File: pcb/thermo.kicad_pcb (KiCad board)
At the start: 2 copper layers, 123.2 x 91.4 mm, 38 parts, among them J1 DB15_Female, J2 Barrel_Jack, U1 BME280

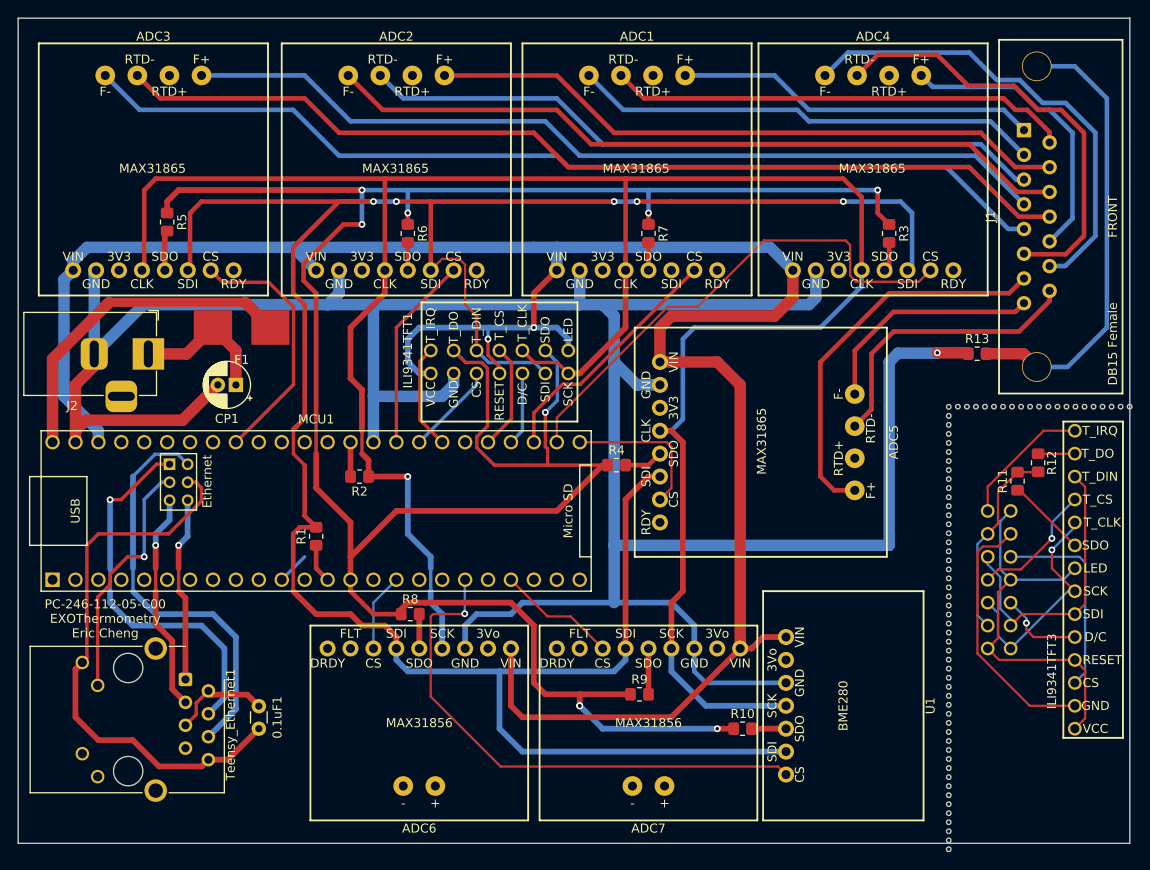
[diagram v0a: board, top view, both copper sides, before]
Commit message: removed acid trap and made some tracer wider
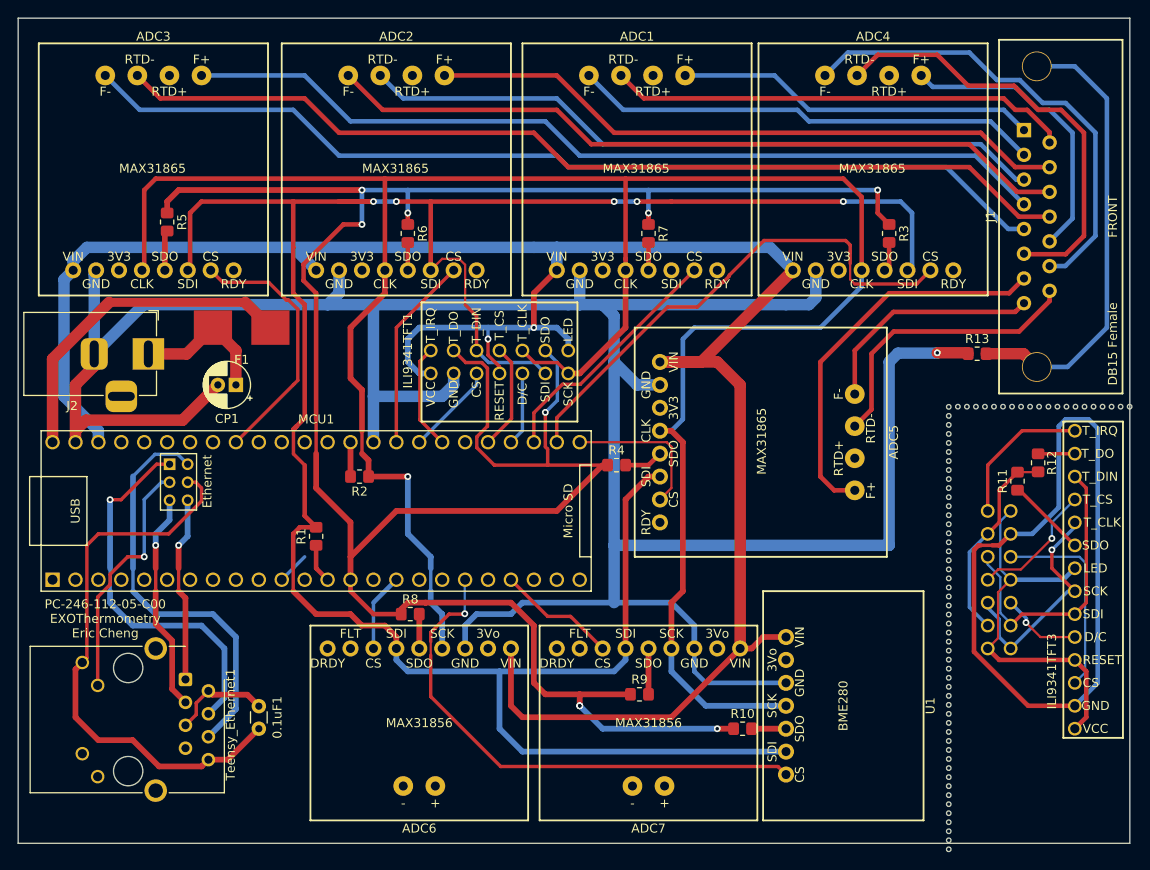
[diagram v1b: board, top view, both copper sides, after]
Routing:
- net GND: track 332.1 -> 385.3 mm
- net +3V3: track 295.1 -> 291.2 mm
- net /SDI: track 315.5 -> 313.5 mm
- net /CS_4: track 56.7 -> 58.4 mm
- net /T_IRQ: track 26.6 -> 28.0 mm
- net /CS_8: track 59.6 -> 58.6 mm
- net /SDO: track 300.6 -> 301.3 mm
- net /CS_3: track 28.5 -> 29.0 mm

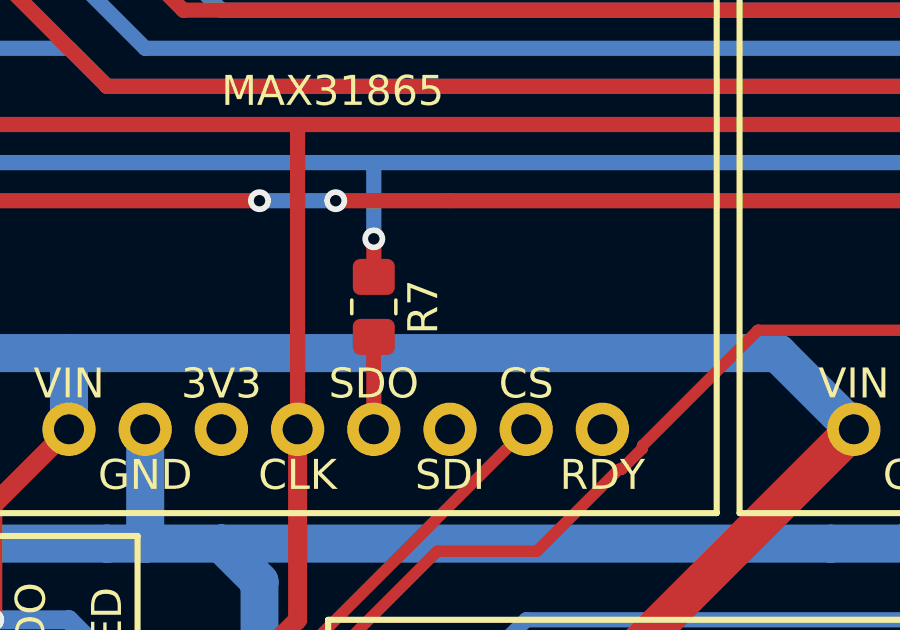
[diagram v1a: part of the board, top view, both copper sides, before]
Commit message: added missing SDI trace for ADC1
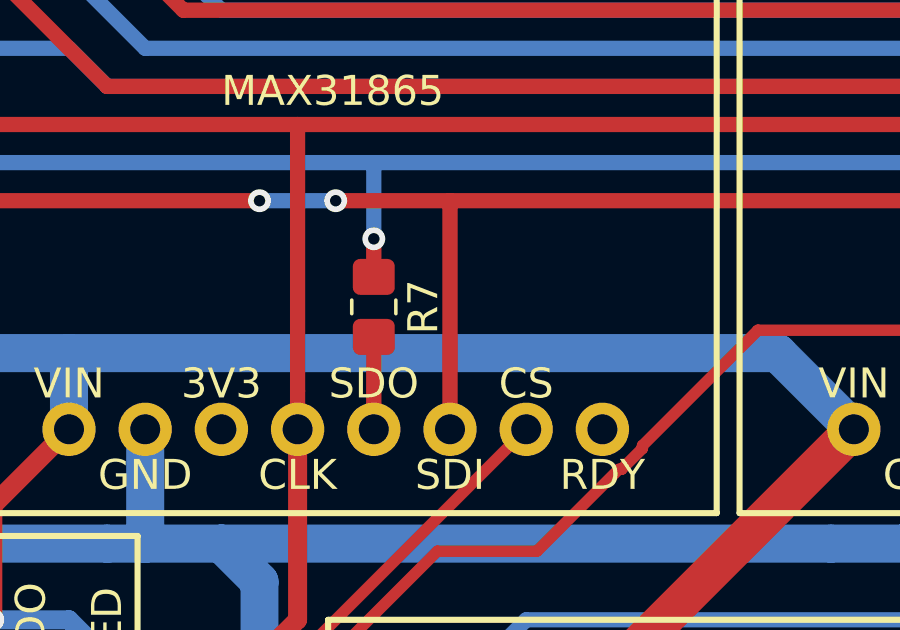
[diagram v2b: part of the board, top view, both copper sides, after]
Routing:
- net /SDI: track 313.5 -> 321.1 mm
